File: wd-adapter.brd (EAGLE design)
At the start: 49.2 x 62.2 mm, 35 parts, among them Q1 BS170, Q2 BS170, Q3 BS170, Q4 BS170, Q5 BS170, Q6 BS170, T1 BC337, X2 KUSBVX

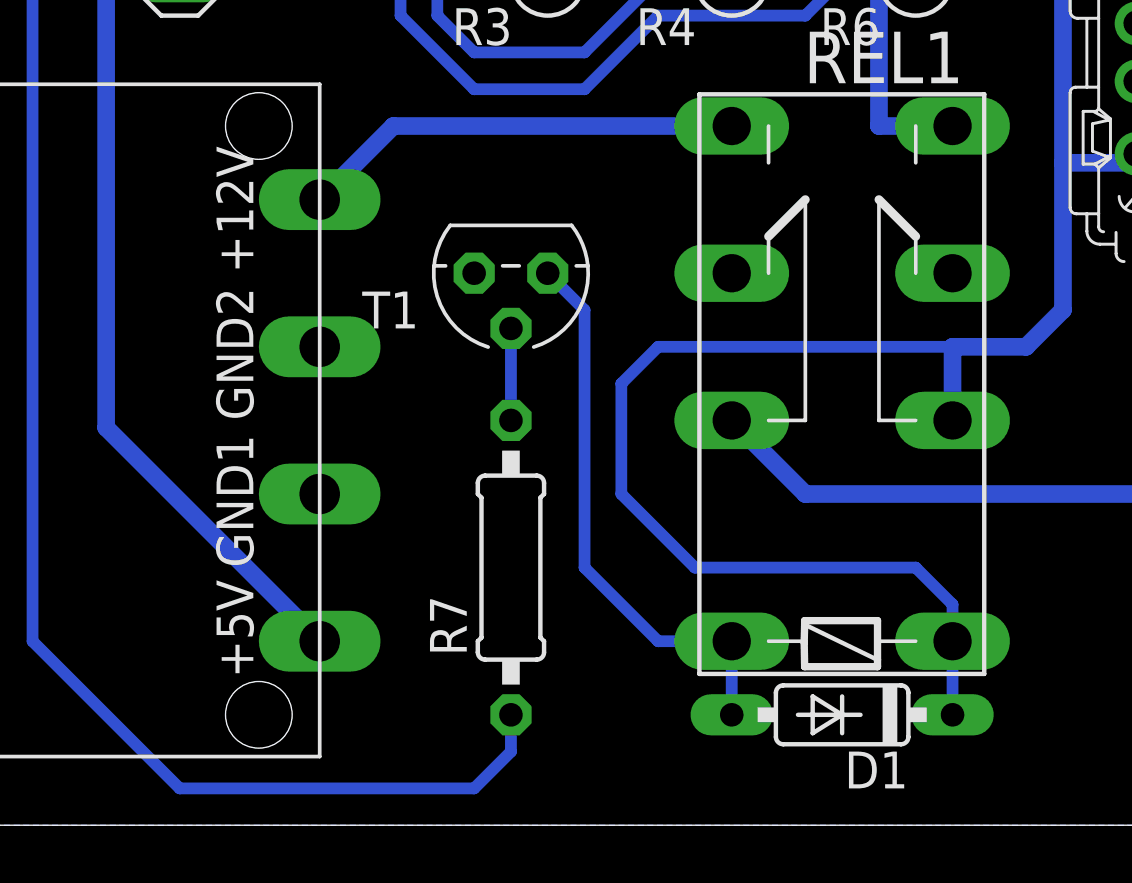
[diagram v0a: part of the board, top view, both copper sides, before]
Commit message: Zustands-LED eingebaut
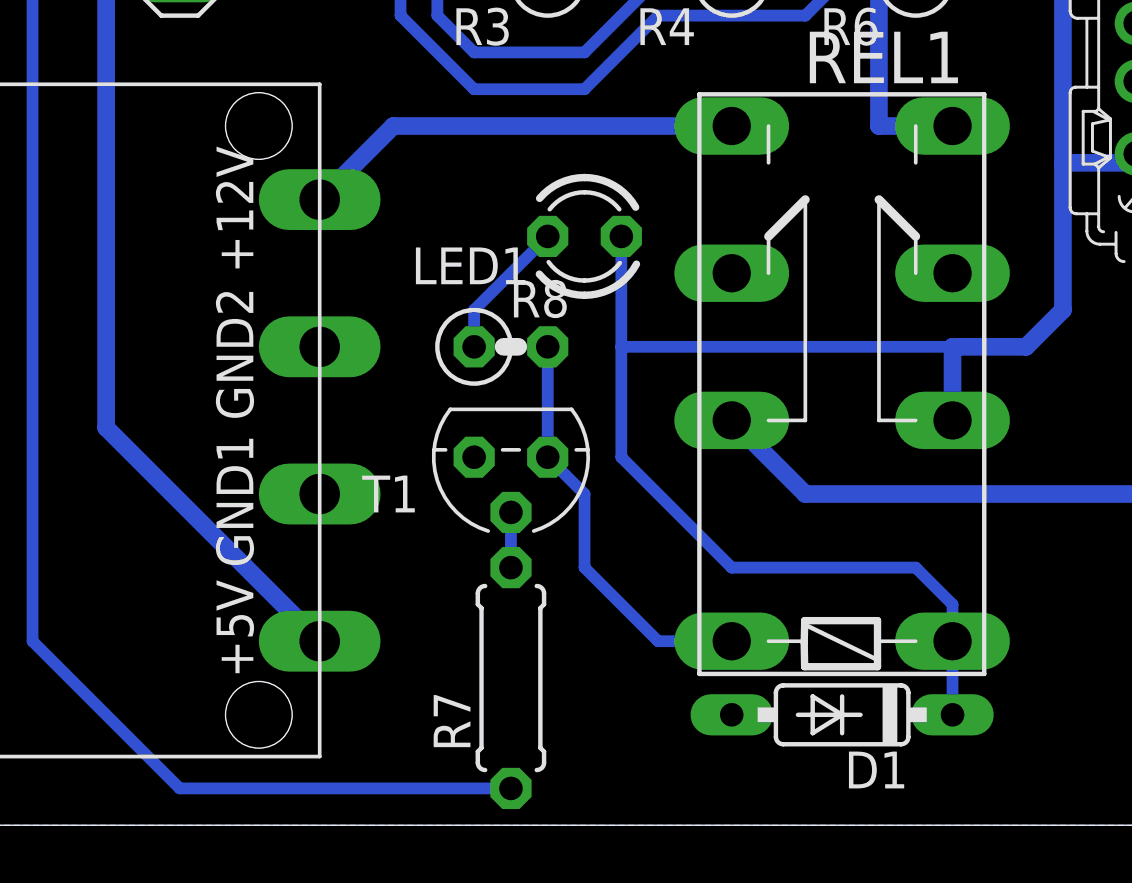
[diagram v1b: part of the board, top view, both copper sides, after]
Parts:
- added LED1: (no value), led:LED3MM
- added R8: 150R, resistor:0207/2V
- R7: device resistor:0207/10 -> resistor:0207/7
- moved T1 6.35 mm to (17.8, 12.7)
- moved R7 3.81 mm to (17.8, 5.08)
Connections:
- removed net N$19: D1.A, REL1.2, T1.3
- new net N$10: LED1.K, R8.1
- new net N$18: D1.A, R8.2, REL1.2, T1.3
- net VCC_IN: now also LED1.A
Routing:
- net N$19: track 19.4 -> 0.00 mm
- net N$18: track 0.00 -> 14.3 mm
- net N$10: track 0.00 -> 4.86 mm
- net VCC_IN: track 83.3 -> 87.1 mm
- net SWITCH: track 98.9 -> 97.1 mm
- net N$20: track 3.17 -> 1.90 mm
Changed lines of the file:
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@@
 <setting verticaltext="up"/>
 </settings>
-<grid distance="0.05" unitdist="inch" unit="inch" style="lines" multiple="1" display="no" altdistance="0.025" altunitdist="inch" altunit="inch"/>
+<grid distance="1.27" unitdist="mm" unit="mm" style="lines" multiple="1" display="no" altdistance="0.025" altunitdist="inch" altunit="inch"/>
 <layers>
 <layer number="1" name="Top" color="4" fill="1" visible="yes" active="yes"/>
@@
 <layer number="37" name="tTest" color="7" fill="1" visible="no" active="yes"/>
 <layer number="38" name="bTest" color="7" fill="1" visible="no" active="yes"/>
-<layer number="39" name="tKeepout" color="4" fill="11" visible="yes" active="yes"/>
-<layer number="40" name="bKeepout" color="1" fill="11" visible="yes" active="yes"/>
-<layer number="41" name="tRestrict" color="4" fill="10" visible="yes" active="yes"/>
-<layer number="42" name="bRestrict" color="1" fill="10" visible="yes" active="yes"/>
-<layer number="43" name="vRestrict" color="2" fill="10" visible="yes" active="yes"/>
-<layer number="44" name="Drills" color="7" fill="1" visible="yes" active="yes"/>
+<layer number="39" name="tKeepout" color="4" fill="11" visible="no" active="yes"/>
+<layer number="40" name="bKeepout" color="1" fill="11" visible="no" active="yes"/>
+<layer number="41" name="tRestrict" color="4" fill="10" visible="no" active="yes"/>
+<layer number="42" name="bRestrict" color="1" fill="10" visible="no" active="yes"/>
+<layer number="43" name="vRestrict" color="2" fill="10" visible="no" active="yes"/>
+<layer number="44" name="Drills" color="7" fill="1" visible="no" active="yes"/>
 <layer number="45" name="Holes" color="7" fill="1" visible="yes" active="yes"/>
-<layer number="46" name="Milling" color="3" fill="1" visible="yes" active="yes"/>
-<layer number="47" name="Measures" color="7" fill="1" visible="yes" active="yes"/>
-<layer number="48" name="Document" color="7" fill="1" visible="yes" active="yes"/>
-<layer number="49" name="Reference" color="7" fill="1" visible="yes" active="yes"/>
+<layer number="46" name="Milling" color="3" fill="1" visible="no" active="yes"/>
+<layer number="47" name="Measures" color="7" fill="1" visible="no" active="yes"/>
+<layer number="48" name="Document" color="7" fill="1" visible="no" active="yes"/>
+<layer number="49" name="Reference" color="7" fill="1" visible="no" active="yes"/>
 <layer number="50" name="dxf" color="7" fill="1" visible="no" active="no"/>
-<layer number="51" name="tDocu" color="7" fill="1" visible="yes" active="yes"/>
-<layer number="52" name="bDocu" color="7" fill="1" visible="yes" active="yes"/>
+<layer number="51" name="tDocu" color="7" fill="1" visible="no" active="yes"/>
+<layer number="52" name="bDocu" color="7" fill="1" visible="no" active="yes"/>
 <layer number="91" name="Nets" color="2" fill="1" visible="no" active="no"/>
 <layer number="92" name="Busses" color="1" fill="1" visible="no" active="no"/>
@@
 <element name="U$1" library="n39" package="PSW_5" value="" x="5.08" y="13.97" rot="R90"/>
 <element name="U$3" library="n39" package="PSW_5" value="" x="46.99" y="49.53" rot="R270"/>
-<element name="T1" library="transistor" package="TO92" value="BC337" x="17.78" y="19.05" rot="R180"/>
+<element name="T1" library="transistor" package="TO92" value="BC337" x="17.78" y="12.7" rot="R180"/>
 <element name="D1" library="diode" package="DO35-7" value="1N4148DO35-7" x="29.21" y="3.81" rot="R180"/>
-<element name="R7" library="resistor" package="0207/10" value="1.5K" x="17.78" y="8.89" rot="R90"/>
+<element name="R7" library="resistor" package="0207/7" value="1.5K" x="17.78" y="5.08" rot="R90"/>
+<element name="LED1" library="led" package="LED3MM" value="" x="20.32" y="20.32" rot="R180"/>
+<element name="R8" library="resistor" package="0207/2V" value="150R" x="17.78" y="16.51"/>
 </elements>
 <signals>
@@
 <wire x1="33.02" y1="6.35" x2="33.02" y2="7.62" width="0.4064" layer="16"/>
 <wire x1="33.02" y1="7.62" x2="31.75" y2="8.89" width="0.4064" layer="16"/>
-<wire x1="31.75" y1="8.89" x2="24.13" y2="8.89" width="0.4064" layer="16"/>
-<wire x1="24.13" y1="8.89" x2="21.59" y2="11.43" width="0.4064" layer="16"/>
-<wire x1="21.59" y1="11.43" x2="21.59" y2="15.24" width="0.4064" layer="16"/>
-<wire x1="21.59" y1="15.24" x2="22.86" y2="16.51" width="0.4064" layer="16"/>
-<wire x1="22.86" y1="16.51" x2="33.02" y2="16.51" width="0.4064" layer="16"/>
+<wire x1="31.75" y1="8.89" x2="25.4" y2="8.89" width="0.4064" layer="16"/>
+<wire x1="25.4" y1="8.89" x2="21.59" y2="12.7" width="0.4064" layer="16"/>
+<wire x1="21.59" y1="16.51" x2="33.02" y2="16.51" width="0.4064" layer="16"/>
 <wire x1="33.02" y1="16.51" x2="35.56" y2="16.51" width="0.6096" layer="16"/>
 <wire x1="33.02" y1="13.97" x2="33.02" y2="16.51" width="0.6096" layer="16"/>
-</signal>
-<signal name="N$19">
-<contactref element="D1" pad="A"/>
-<contactref element="REL1" pad="2"/>
-<contactref element="T1" pad="3"/>
-<wire x1="25.4" y1="6.35" x2="25.4" y2="3.81" width="0.4064" layer="16"/>
-<wire x1="19.05" y1="19.05" x2="20.32" y2="17.78" width="0.4064" layer="16"/>
-<wire x1="20.32" y1="17.78" x2="20.32" y2="8.89" width="0.4064" layer="16"/>
-<wire x1="20.32" y1="8.89" x2="22.86" y2="6.35" width="0.4064" layer="16"/>
-<wire x1="22.86" y1="6.35" x2="25.4" y2="6.35" width="0.4064" layer="16"/>
+<contactref element="LED1" pad="A"/>
+<wire x1="21.59" y1="20.32" x2="21.59" y2="16.51" width="0.4064" layer="16"/>
+<wire x1="21.59" y1="16.51" x2="21.59" y2="12.7" width="0.4064" layer="16"/>
 </signal>
 <signal name="N$20">
 <contactref element="R7" pad="2"/>
 <contactref element="T1" pad="2"/>
-<wire x1="17.78" y1="17.145" x2="17.78" y2="13.97" width="0.4064" layer="16"/>
+<wire x1="17.78" y1="10.795" x2="17.78" y2="8.89" width="0.4064" layer="16"/>
 </signal>
 <signal name="SWITCH">
@@
 <wire x1="1.27" y1="58.42" x2="1.27" y2="6.35" width="0.4064" layer="16"/>
 <wire x1="1.27" y1="6.35" x2="6.35" y2="1.27" width="0.4064" layer="16"/>
-<wire x1="6.35" y1="1.27" x2="16.51" y2="1.27" width="0.4064" layer="16"/>
-<wire x1="16.51" y1="1.27" x2="17.78" y2="2.54" width="0.4064" layer="16"/>
-<wire x1="17.78" y1="2.54" x2="17.78" y2="3.81" width="0.4064" layer="16"/>
+<wire x1="6.35" y1="1.27" x2="17.78" y2="1.27" width="0.4064" layer="16"/>
 <wire x1="2.54" y1="59.69" x2="1.27" y2="58.42" width="0.4064" layer="16"/>
 </signal>
@@
 <wire x1="44.45" y1="41.91" x2="40.89" y2="41.91" width="0.6096" layer="16"/>
 </signal>
+<signal name="N$10">
+<contactref element="LED1" pad="K"/>
+<contactref element="R8" pad="1"/>
+<wire x1="16.51" y1="16.51" x2="16.51" y2="17.78" width="0.4064" layer="16"/>
+<wire x1="16.51" y1="17.78" x2="19.05" y2="20.32" width="0.4064" layer="16"/>
+</signal>
+<signal name="N$18">
+<contactref element="D1" pad="A"/>
+<contactref element="R8" pad="2"/>
+<contactref element="REL1" pad="2"/>
+<contactref element="T1" pad="3"/>
+<wire x1="19.05" y1="12.7" x2="20.32" y2="11.43" width="0.4064" layer="16"/>
+<wire x1="20.32" y1="11.43" x2="20.32" y2="8.89" width="0.4064" layer="16"/>
+<wire x1="20.32" y1="8.89" x2="22.86" y2="6.35" width="0.4064" layer="16"/>
+<wire x1="22.86" y1="6.35" x2="25.4" y2="6.35" width="0.4064" layer="16"/>
+<wire x1="19.05" y1="12.7" x2="19.05" y2="16.51" width="0.4064" layer="16"/>
+<wire x1="25.4" y1="6.35" x2="25.4" y2="3.81" width="0" layer="19" extent="1-1"/>
+</signal>
 </signals>
